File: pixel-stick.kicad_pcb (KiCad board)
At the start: 2 copper layers, 42 x 20.5 mm, 19 parts, among them J1 WS281*, J2 UART, Q1 BSS138, U1 LM3670MF, U2 RT9361A, U3 ESP-01v090, U4 ESP-M2

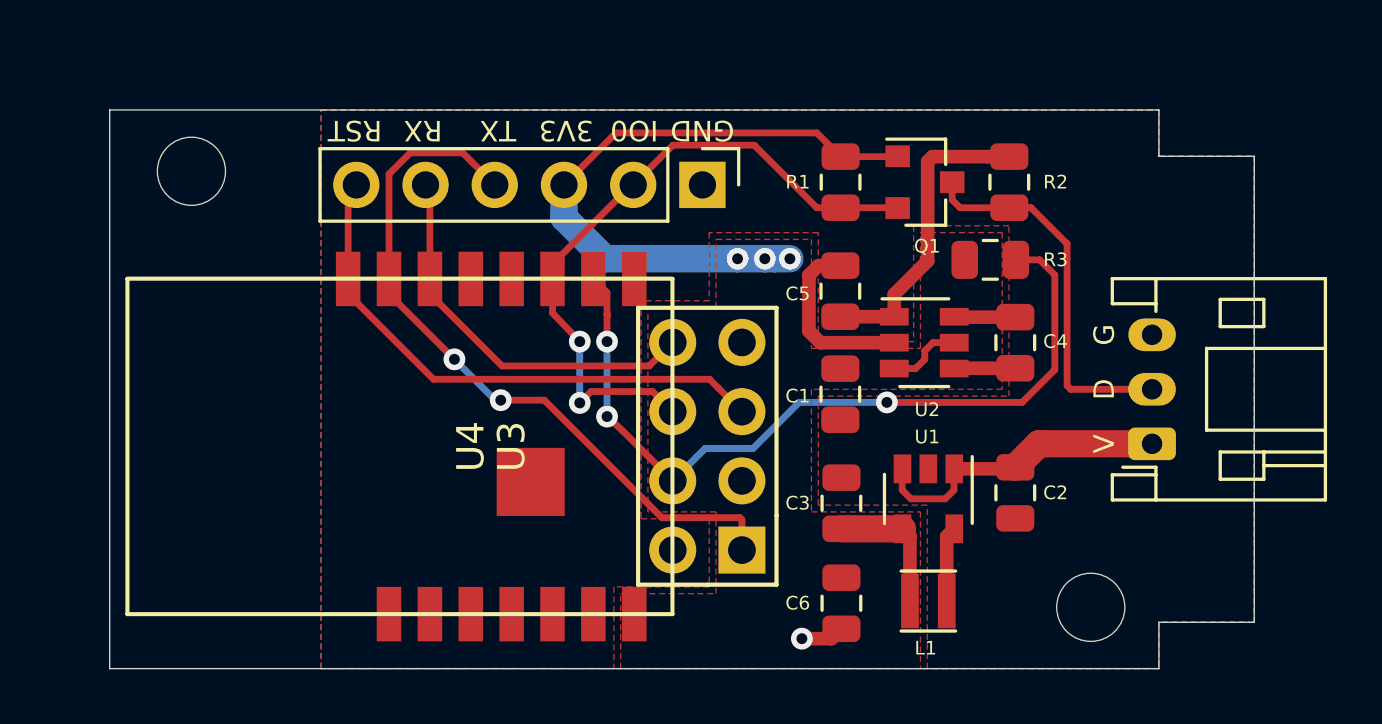
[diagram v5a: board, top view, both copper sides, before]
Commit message: add pull-up for reset and enable
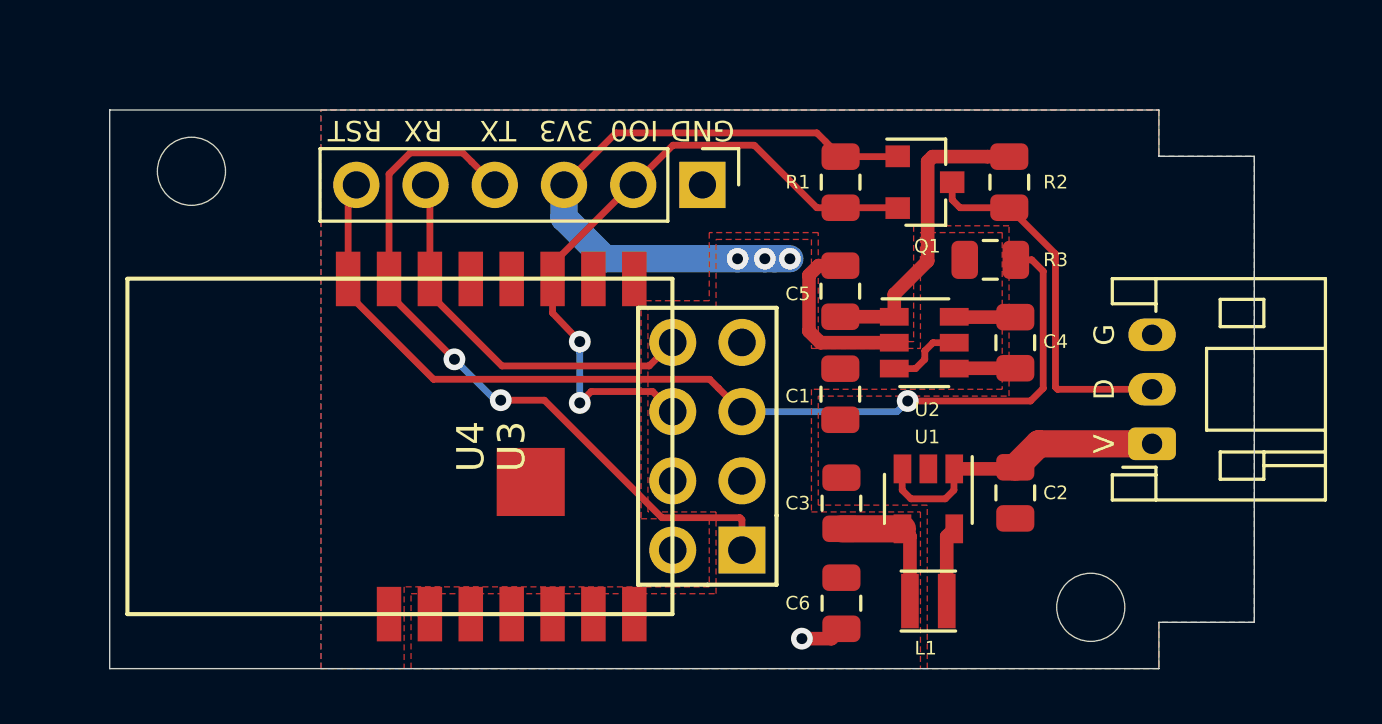
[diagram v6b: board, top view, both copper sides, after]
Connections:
- R3 pad 2: /GPIO2 -> /RST
- U3 pad 3: Net-(U3-Pad3) -> +3V3
- U3 pad 4: /GPIO2 -> Net-(U3-Pad4)
- U4 pad 2: Net-(U4-Pad2) -> +3V3
- U4 pad 9: /GPIO2 -> Net-(U4-Pad9)
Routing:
- net /GPIO2: track 30.8 -> 0.00 mm, vias 3 -> 0
- net /RST: track 19.8 -> 36.7 mm, vias 0 -> 1

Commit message: upgrade 3.3v regulator
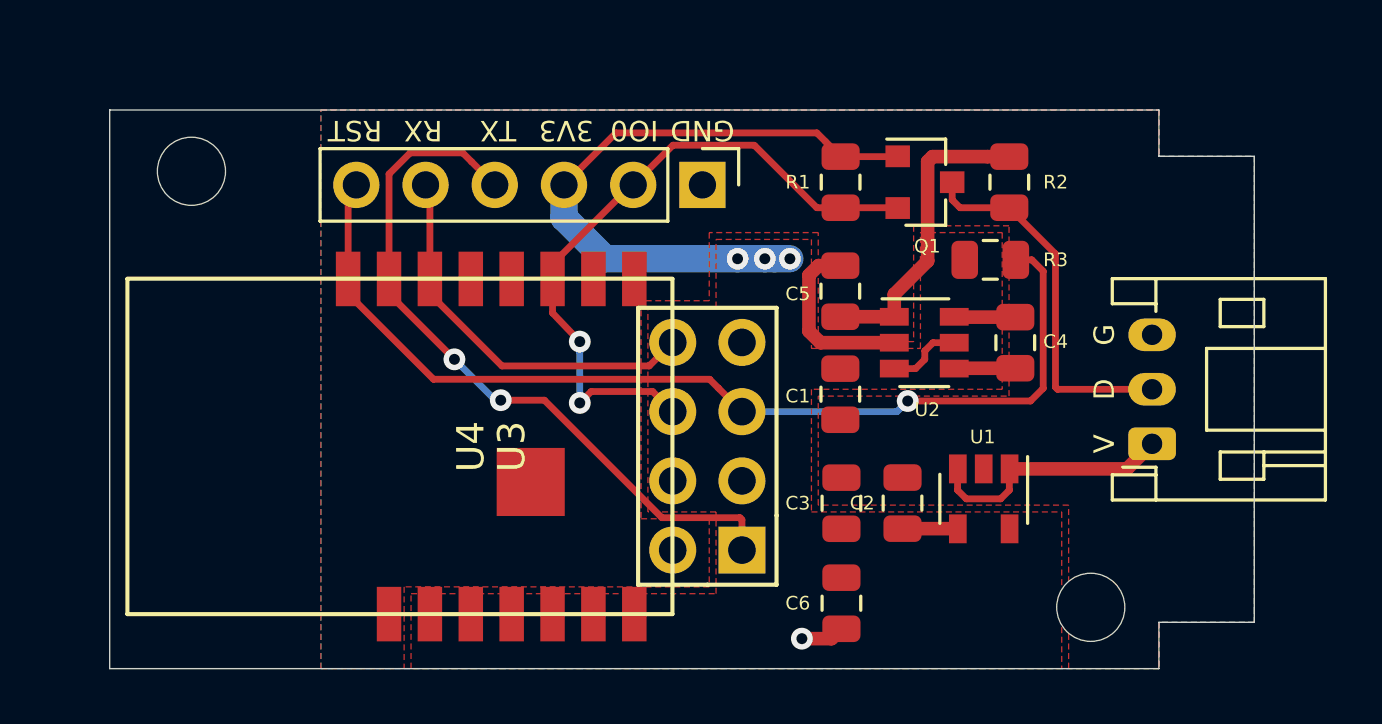
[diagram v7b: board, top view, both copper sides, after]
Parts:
- removed L1: 2.2uH, Inductor_SMD:L_Taiyo-Yuden_MD-2020
- U1: value LM3670MF -> SPX3819M5-L-3-3
- moved C2 4.16 mm to (101.1, 42.9), turned to 90 degrees
- moved U1 2.03 mm to (104.1, 42.8)
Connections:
- C2 pad 1: VIN -> Net-(C2-Pad1)
- U1 pad 4: +3V3 -> Net-(C2-Pad1)
- U1 pad 5: Net-(L1-Pad1) -> +3V3
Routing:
- net +3V3: track 31.4 -> 26.4 mm
- net Net-(L1-Pad1): track 2.76 -> 0.00 mm
- net VIN: track 11.3 -> 9.08 mm
- net Net-(C2-Pad1): track 0.00 -> 2.03 mm

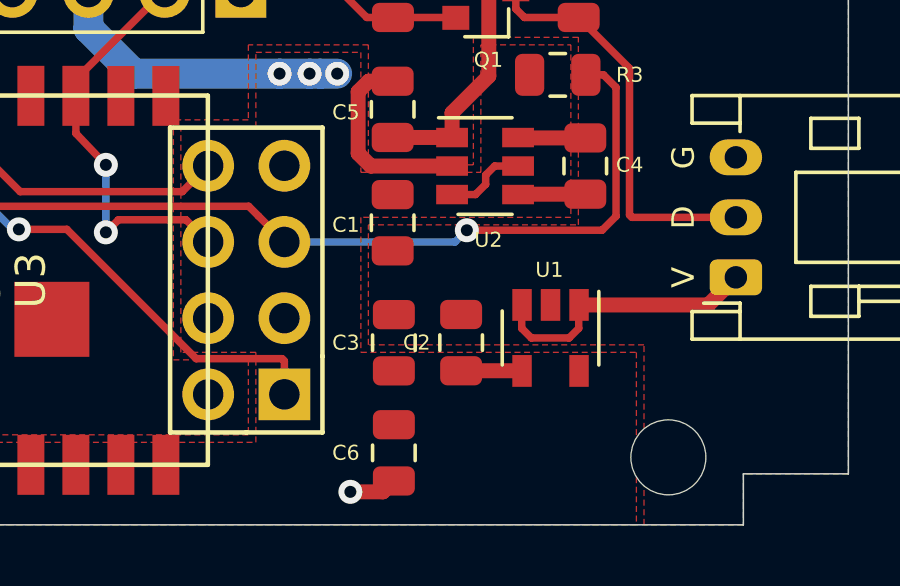
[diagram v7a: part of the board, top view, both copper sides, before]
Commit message: consolidate capacitors
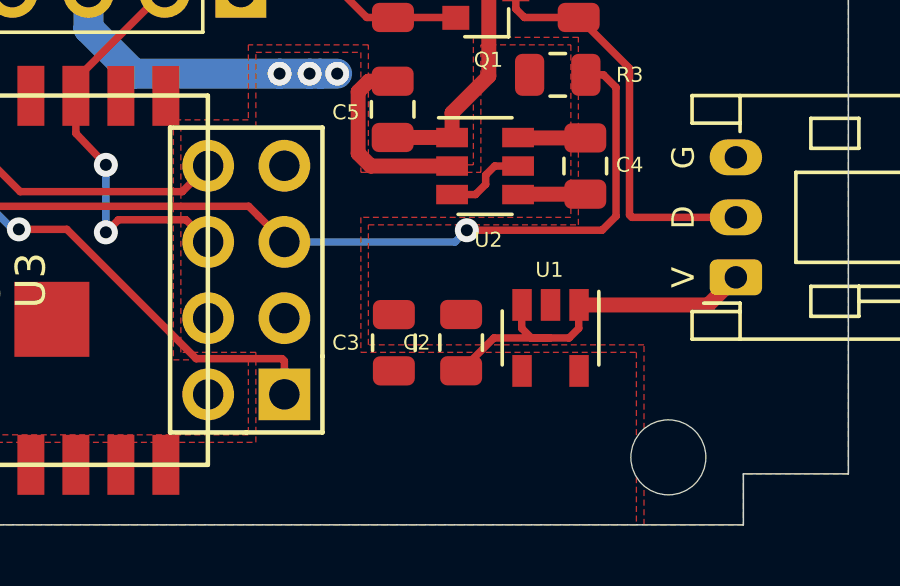
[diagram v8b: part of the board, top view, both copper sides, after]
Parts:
- removed C1: 10µF, Capacitor_SMD:C_0805_2012Metric
- removed C6: 22µF, Capacitor_SMD:C_0805_2012Metric
- C3: value 22µF -> 10µF
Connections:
- C2 pad 1: Net-(C2-Pad1) -> VIN
- U1 pad 4: Net-(C2-Pad1) -> Net-(U1-Pad4)
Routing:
- net VIN: track 9.08 -> 12.5 mm
- net Net-(C2-Pad1): track 2.03 -> 0.00 mm
- net GND: track 8.26 -> 6.66 mm, vias 1 -> 0
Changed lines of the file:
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@@
     (thickness 1.6)
     (drawings 21)
-    (tracks 120)
+    (tracks 118)
     (zones 0)
-    (modules 18)
+    (modules 16)
     (nets 22)
   )
@@
   )
   (setup
-    (last_trace_width 0.5)
+    (last_trace_width 0.25)
     (user_trace_width 0.5)
     (user_trace_width 1)
@@
   (net 19 "Net-(U3-Pad4)")
   (net 20 "Net-(U4-Pad9)")
-  (net 21 "Net-(C2-Pad1)")
+  (net 21 "Net-(U1-Pad4)")
   (net_class Default "This is the default net class."
     (clearance 0.2)
@@
     (add_net /TXD)
     (add_net GND)
-    (add_net "Net-(C2-Pad1)")
     (add_net "Net-(C4-Pad1)")
     (add_net "Net-(C4-Pad2)")
+    (add_net "Net-(U1-Pad4)")
     (add_net "Net-(U3-Pad4)")
     (add_net "Net-(U4-Pad1)")
@@
       (net 2 +3V3))
     (pad 4 smd rect (at 1.1 0.95 270) (size 1.06 0.65) (layers F.Cu F.Paste F.Mask)
-      (net 21 "Net-(C2-Pad1)"))
+      (net 21 "Net-(U1-Pad4)"))
     (pad 3 smd rect (at -1.1 0.95 270) (size 1.06 0.65) (layers F.Cu F.Paste F.Mask)
       (net 8 VIN))
@@
       (net 8 VIN))
     (model ${KISYS3DMOD}/Package_TO_SOT_SMD.3dshapes/SOT-23-5.wrl
-      (at (xyz 0 0 0))
-      (scale (xyz 1 1 1))
-      (rotate (xyz 0 0 0))
-    )
-  )
-  (module Capacitor_SMD:C_0805_2012Metric locked (layer F.Cu)
-    (at 98.85 46.6 90)
-    (descr "Capacitor SMD 0805 (2012 Metric), square (rectangular) end terminal, IPC_7351 nominal, (Body size source: https://docs.google.com/spreadsheets/d/1BsfQQcO9C6DZCsRaXUlFlo91Tg2WpOkGARC1WS5S8t0/edit?usp=sharing), generated with kicad-footprint-generator")
-    (tags capacitor)
-    (attr smd)
-    (fp_text reference C6 (at 0 -1.6 180) (layer F.SilkS)
-      (effects (font (size 0.5 0.5) (thickness 0.125)))
-    )
-    (fp_text value 22µF (at 0 1.65 90) (layer F.Fab)
-      (effects (font (size 1 1) (thickness 0.15)))
-    )
-    (fp_text user %R (at 0 0 90) (layer F.Fab)
-      (effects (font (size 0.5 0.5) (thickness 0.08)))
-    )
-    (fp_line (start 1.68 0.95) (end -1.68 0.95) (layer F.CrtYd) (width 0.05))
-    (fp_line (start 1.68 -0.95) (end 1.68 0.95) (layer F.CrtYd) (width 0.05))
-    (fp_line (start -1.68 -0.95) (end 1.68 -0.95) (layer F.CrtYd) (width 0.05))
-    (fp_line (start -1.68 0.95) (end -1.68 -0.95) (layer F.CrtYd) (width 0.05))
-    (fp_line (start -0.258578 0.71) (end 0.258578 0.71) (layer F.SilkS) (width 0.12))
-    (fp_line (start -0.258578 -0.71) (end 0.258578 -0.71) (layer F.SilkS) (width 0.12))
-    (fp_line (start 1 0.6) (end -1 0.6) (layer F.Fab) (width 0.1))
-    (fp_line (start 1 -0.6) (end 1 0.6) (layer F.Fab) (width 0.1))
-    (fp_line (start -1 -0.6) (end 1 -0.6) (layer F.Fab) (width 0.1))
-    (fp_line (start -1 0.6) (end -1 -0.6) (layer F.Fab) (width 0.1))
-    (pad 2 smd roundrect (at 0.9375 0 90) (size 0.975 1.4) (layers F.Cu F.Paste F.Mask) (roundrect_rratio 0.25)
-      (net 2 +3V3))
-    (pad 1 smd roundrect (at -0.9375 0 90) (size 0.975 1.4) (layers F.Cu F.Paste F.Mask) (roundrect_rratio 0.25)
-      (net 1 GND))
-    (model ${KISYS3DMOD}/Capacitor_SMD.3dshapes/C_0805_2012Metric.wrl
       (at (xyz 0 0 0))
       (scale (xyz 1 1 1))
@@
       (effects (font (size 0.5 0.5) (thickness 0.125)))
     )
-    (fp_text value 22µF (at 0 1.65 90) (layer F.Fab)
+    (fp_text value 10µF (at 0 1.65 90) (layer F.Fab)
       (effects (font (size 1 1) (thickness 0.15)))
     )
@@
     )
     (pad 1 smd roundrect (at -0.9375 0 90) (size 0.975 1.4) (layers F.Cu F.Paste F.Mask) (roundrect_rratio 0.25)
-      (net 21 "Net-(C2-Pad1)"))
+      (net 8 VIN))
     (pad 2 smd roundrect (at 0.9375 0 90) (size 0.975 1.4) (layers F.Cu F.Paste F.Mask) (roundrect_rratio 0.25)
       (net 1 GND))
-    (model ${KISYS3DMOD}/Capacitor_SMD.3dshapes/C_0805_2012Metric.wrl
-      (at (xyz 0 0 0))
-      (scale (xyz 1 1 1))
-      (rotate (xyz 0 0 0))
-    )
-  )
-  (module Capacitor_SMD:C_0805_2012Metric (layer F.Cu)
-    (at 98.81 38.93 270)
-    (descr "Capacitor SMD 0805 (2012 Metric), square (rectangular) end terminal, IPC_7351 nominal, (Body size source: https://docs.google.com/spreadsheets/d/1BsfQQcO9C6DZCsRaXUlFlo91Tg2WpOkGARC1WS5S8t0/edit?usp=sharing), generated with kicad-footprint-generator")
-    (tags capacitor)
-    (attr smd)
-    (fp_text reference C1 (at 0.07 1.56 180) (layer F.SilkS)
-      (effects (font (size 0.5 0.5) (thickness 0.125)))
-    )
-    (fp_text value 10µF (at 0 1.65 90) (layer F.Fab)
-      (effects (font (size 1 1) (thickness 0.15)))
-    )
-    (fp_text user %R (at 0 0 90) (layer F.Fab)
-      (effects (font (size 0.5 0.5) (thickness 0.08)))
-    )
-    (fp_line (start 1.68 0.95) (end -1.68 0.95) (layer F.CrtYd) (width 0.05))
-    (fp_line (start 1.68 -0.95) (end 1.68 0.95) (layer F.CrtYd) (width 0.05))
-    (fp_line (start -1.68 -0.95) (end 1.68 -0.95) (layer F.CrtYd) (width 0.05))
-    (fp_line (start -1.68 0.95) (end -1.68 -0.95) (layer F.CrtYd) (width 0.05))
-    (fp_line (start -0.258578 0.71) (end 0.258578 0.71) (layer F.SilkS) (width 0.12))
-    (fp_line (start -0.258578 -0.71) (end 0.258578 -0.71) (layer F.SilkS) (width 0.12))
-    (fp_line (start 1 0.6) (end -1 0.6) (layer F.Fab) (width 0.1))
-    (fp_line (start 1 -0.6) (end 1 0.6) (layer F.Fab) (width 0.1))
-    (fp_line (start -1 -0.6) (end 1 -0.6) (layer F.Fab) (width 0.1))
-    (fp_line (start -1 0.6) (end -1 -0.6) (layer F.Fab) (width 0.1))
-    (pad 2 smd roundrect (at 0.9375 0 270) (size 0.975 1.4) (layers F.Cu F.Paste F.Mask) (roundrect_rratio 0.25)
-      (net 1 GND))
-    (pad 1 smd roundrect (at -0.9375 0 270) (size 0.975 1.4) (layers F.Cu F.Paste F.Mask) (roundrect_rratio 0.25)
-      (net 2 +3V3))
     (model ${KISYS3DMOD}/Capacitor_SMD.3dshapes/C_0805_2012Metric.wrl
       (at (xyz 0 0 0))
@@
   (segment (start 98.081374 37.04) (end 97.65999 36.618616) (width 0.5) (layer F.Cu) (net 1))
   (segment (start 100.79 37.04) (end 98.081374 37.04) (width 0.5) (layer F.Cu) (net 1))
-  (via (at 97.4 47.9) (size 0.8) (drill 0.4) (layers F.Cu B.Cu) (net 1))
-  (segment (start 98.4875 47.9) (end 98.85 47.5375) (width 0.5) (layer F.Cu) (net 1))
-  (segment (start 97.4 47.9) (end 98.4875 47.9) (width 0.5) (layer F.Cu) (net 1))
   (segment (start 98.8525 43.87) (end 98.85 43.8675) (width 0.5) (layer F.Cu) (net 2))
   (segment (start 100.785 37.995) (end 100.79 37.99) (width 0.5) (layer F.Cu) (net 2))
@@
   (segment (start 90.577509 29.342491) (end 97.949991 29.342491) (width 0.25) (layer F.Cu) (net 2))
   (segment (start 88.67 31.25) (end 90.577509 29.342491) (width 0.25) (layer F.Cu) (net 2))
-  (segment (start 80.75 34.7) (end 80.75 31.55) (width 0.25) (layer F.Cu) (net 12))
-  (segment (start 80.75 31.55) (end 81.05 31.25) (width 0.25) (layer F.Cu) (net 12))
-  (segment (start 80.75 35.25) (end 83.881399 38.381399) (width 0.25) (layer F.Cu) (net 12))
-  (segment (start 83.881399 38.381399) (end 94.011399 38.381399) (width 0.25) (layer F.Cu) (net 12))
-  (segment (start 94.011399 38.381399) (end 94.336401 38.706401) (width 0.25) (layer F.Cu) (net 12))
-  (segment (start 94.336401 38.706401) (end 95.2 39.57) (width 0.25) (layer F.Cu) (net 12))
   (segment (start 100.785 36.085) (end 100.79 36.09) (width 0.5) (layer F.Cu) (net 3))
   (segment (start 100.7875 36.0875) (end 100.79 36.09) (width 0.5) (layer F.Cu) (net 3))
@@
   (segment (start 105.012 42.45) (end 105.012 41.67) (width 0.25) (layer F.Cu) (net 8))
   (segment (start 104.692 42.77) (end 105.012 42.45) (width 0.25) (layer F.Cu) (net 8))
-  (segment (start 103.432 42.77) (end 104.692 42.77) (width 0.25) (layer F.Cu) (net 8))
   (segment (start 109.33 41.67) (end 110.25 40.75) (width 0.5) (layer F.Cu) (net 8))
   (segment (start 105.276 41.67) (end 109.33 41.67) (width 0.5) (layer F.Cu) (net 8))
+  (segment (start 102.1855 42.77) (end 104.042 42.77) (width 0.25) (layer F.Cu) (net 8))
+  (segment (start 101.092 43.8635) (end 102.1855 42.77) (width 0.25) (layer F.Cu) (net 8))
+  (segment (start 104.042 42.77) (end 104.692 42.77) (width 0.25) (layer F.Cu) (net 8))
+  (segment (start 103.432 42.77) (end 104.042 42.77) (width 0.25) (layer F.Cu) (net 8))
   (segment (start 91.796401 37.893599) (end 92.66 37.03) (width 0.25) (layer F.Cu) (net 9))
   (segment (start 86.393599 37.893599) (end 91.796401 37.893599) (width 0.25) (layer F.Cu) (net 9))
@@
   (segment (start 82.25 30.850998) (end 83.025999 30.074999) (width 0.25) (layer F.Cu) (net 10))
   (segment (start 82.25 34.7) (end 82.25 30.850998) (width 0.25) (layer F.Cu) (net 10))
+  (segment (start 80.75 34.7) (end 80.75 31.55) (width 0.25) (layer F.Cu) (net 12))
+  (segment (start 80.75 31.55) (end 81.05 31.25) (width 0.25) (layer F.Cu) (net 12))
+  (segment (start 80.75 35.25) (end 83.881399 38.381399) (width 0.25) (layer F.Cu) (net 12))
+  (segment (start 83.881399 38.381399) (end 94.011399 38.381399) (width 0.25) (layer F.Cu) (net 12))
+  (segment (start 94.011399 38.381399) (end 94.336401 38.706401) (width 0.25) (layer F.Cu) (net 12))
+  (segment (start 94.336401 38.706401) (end 95.2 39.57) (width 0.25) (layer F.Cu) (net 12))
   (segment (start 106.25501 34.41751) (end 105.8375 34) (width 0.25) (layer F.Cu) (net 12))
   (segment (start 106.25501 38.71549) (end 106.25501 34.41751) (width 0.25) (layer F.Cu) (net 12))
@@
   (segment (start 100.892 39.57) (end 101.2825 39.1795) (width 0.25) (layer B.Cu) (net 12))
   (segment (start 95.2 39.57) (end 100.892 39.57) (width 0.25) (layer B.Cu) (net 12))
-  (segment (start 103.1155 43.8635) (end 103.122 43.87) (width 0.5) (layer F.Cu) (net 21))
-  (segment (start 101.092 43.8635) (end 103.1155 43.8635) (width 0.5) (layer F.Cu) (net 21))
   (zone (net 1) (net_name GND) (layer B.Cu) (hatch edge 0.508)
     (connect_pads (clearance 0.5))
